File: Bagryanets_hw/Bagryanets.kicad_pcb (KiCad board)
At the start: 2 copper layers, 60 x 79 mm, 108 parts, among them U1 SX1276

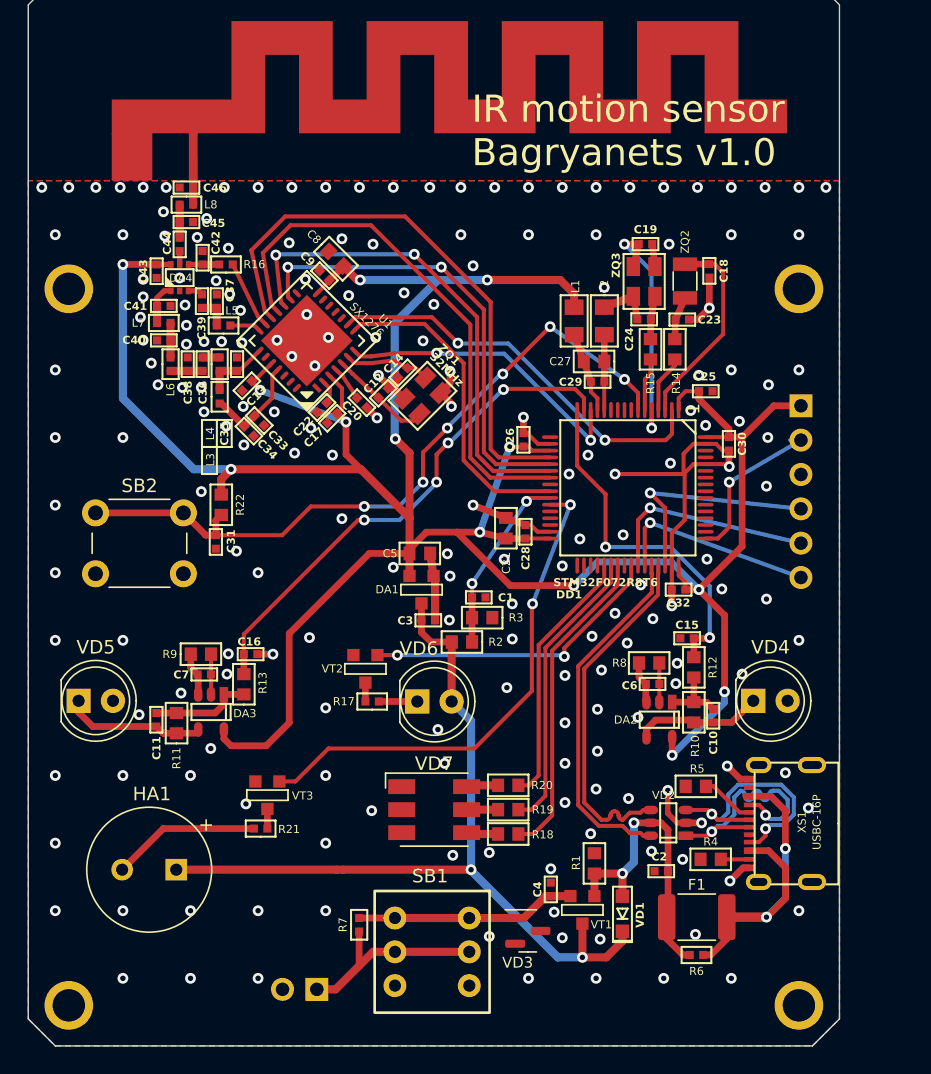
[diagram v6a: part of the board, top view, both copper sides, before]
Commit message: Added bom, small schematic changes
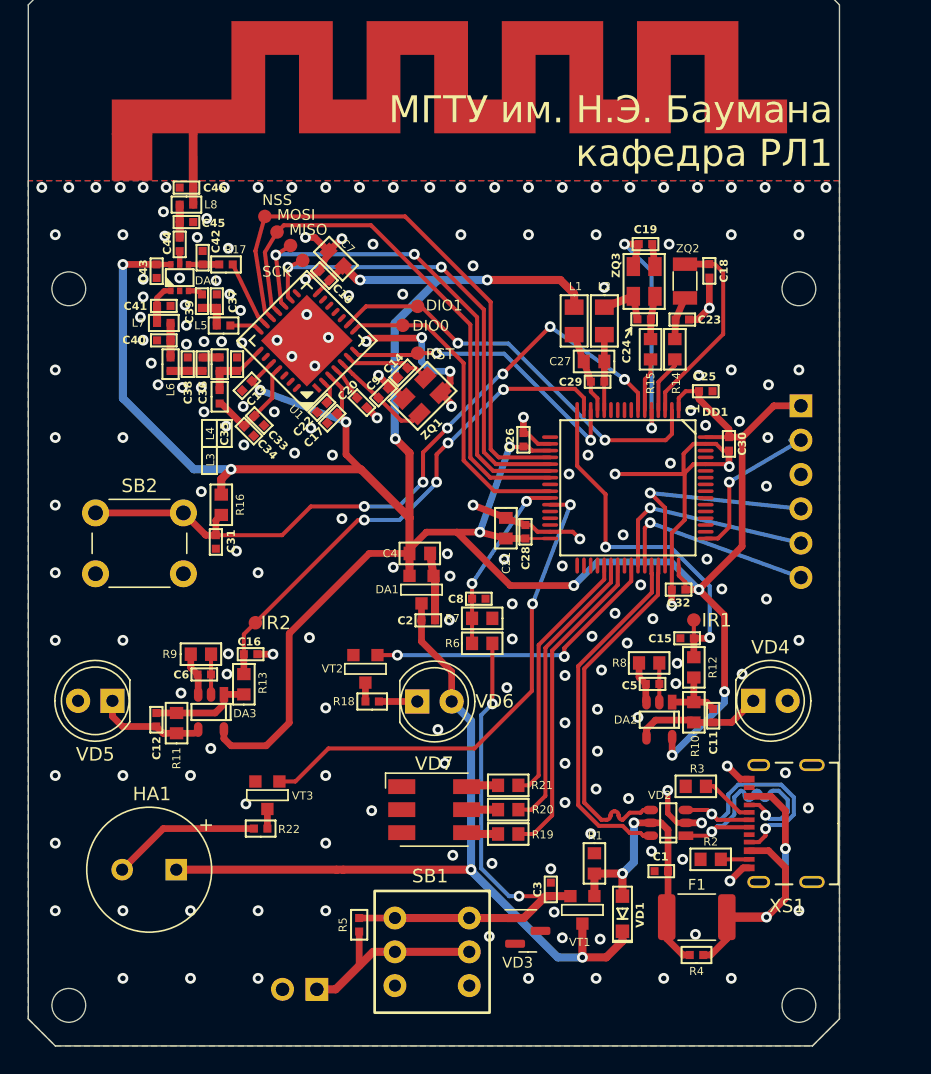
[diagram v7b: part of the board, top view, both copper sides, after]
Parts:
- removed the C1 at (141.3, 96.8)
- removed the R2 at (140.1, 100.1)
- removed the R3 at (141.6, 98.3)
- added C8: 100n, Capacitors:CAP_0402, F.Cu at (141.3, 96.9)
- added R6: 100k, Resistors:RES_0603, F.Cu at (141.6, 100.2)
- added R7: 100k, Resistors:RES_0603, F.Cu at (141.6, 98.4)
- added TP1: TestPoint, PCB:TESTPOINT_1MM, F.Cu at (157.2, 98.5)
- added TP2: TestPoint, PCB:TESTPOINT_1MM, F.Cu at (124.8, 98.7)
- added TP3: TestPoint, PCB:TESTPOINT_1MM, F.Cu at (135.7, 76.7)
- added TP4: TestPoint, PCB:TESTPOINT_1MM, F.Cu at (136.8, 75.3)
- added TP5: TestPoint, PCB:TESTPOINT_1MM, F.Cu at (128.3, 71.9)
- added TP6: TestPoint, PCB:TESTPOINT_1MM, F.Cu at (127.4, 70.8)
- added TP7: TestPoint, PCB:TESTPOINT_1MM, F.Cu at (126.4, 69.8)
- added TP8: TestPoint, PCB:TESTPOINT_1MM, F.Cu at (125.5, 68.7)
- added TP9: TestPoint, PCB:TESTPOINT_1MM, F.Cu at (136.8, 78.8)
- C14, C19, C24: value 10p -> 8p
- C18, C23: value 12.5p -> 9p
- C9: renamed from C12; value 10p -> 8p
- H1, H2, H3, H4: footprint Kais_Lib:Hole_2.4 -> MountingHole:MountingHole_2.5mm
- R22: renamed from R21; value 200 -> 510
- moved VD5 2.50 mm to (114.2, 104.5), turned to 180 degrees
- renumbered C2 to C1, C9 to C10, C10 to C11, C11 to C12, C3 to C2, C4 to C3, C5 to C4, C6 to C5, C7 to C6, C8 to C7, R22 to R16, R16 to R17, R17 to R18, R18 to R19, R4 to R2, R19 to R20, R20 to R21, R5 to R3, R6 to R4, R7 to R5
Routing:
- net /Battery: track 16.3 -> 39.3 mm, vias 0 -> 2
- net GND: track 73.9 -> 91.0 mm, vias 194 -> 192
- net Net-(DA3--): track 10.5 -> 8.13 mm
- net /IR_IN2: track 26.3 -> 27.6 mm
- net /L.MISO: track 36.8 -> 38.1 mm
- net /L.SCK: track 34.1 -> 35.3 mm
- net /Unst.power: track 61.6 -> 60.7 mm
- net /L.DIO1: track 29.9 -> 30.6 mm
- net /L.NSS: track 42.2 -> 42.8 mm
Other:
- board text added: "3.3 B"
- board text added: "DIO0"
- board text added: "DIO1"
- board text added: "GND"
- board text added: "IR1"
- board text added: "IR2"
- board text added: "MISO"
- board text added: "MOSI"
- board text added: "NSS"
- board text added: "RST"
- board text added: "SCK"
- board text added: "SWCLK"
- board text added: "SWDIO"
- board text added: "UART RX"
- board text added: "UART TX"
- board text added: "МГТУ им. Н.Э. Баумана кафедра РЛ1"

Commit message: Schematic update, IR amplifier working
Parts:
- C11, C12: value 1p* -> 8p
- DA1: value MCP1700-3302E_SOT23 -> MCP1700-3302
- DA2, DA3: value LMV721M5 -> MCP6001UT-I/OT
- VD2: value USBLC6_2SC6 -> USBLC6-2SC6
- VD4, VD5: value BL-L515 -> SFH213FA
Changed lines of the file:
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@@
         (effects (font (size 0.6 0.6) (thickness 0.15) bold))
     )
-    (fp_text value "1p*" (at 0 1.15 90) (layer "F.SilkS") hide
+    (fp_text value "8p" (at 0 1.15 90) (layer "F.SilkS") hide
         (effects (font (size 0.6 0.6) (thickness 0.15)))
     )
@@
         (effects (font (size 0.6 0.6) (thickness 0.15)))
     )
-    (fp_text value "MCP1700-3302E_SOT23" (at 0.25 -2.39942) (layer "F.SilkS") hide
+    (fp_text value "MCP1700-3302" (at 0.25 -2.39942) (layer "F.SilkS") hide
         (effects (font (size 0.6 0.6) (thickness 0.15) bold))
     )
@@
         (effects (font (size 1 1) (thickness 0.15)))
     )
-    (fp_text value "BL-L515" (at 1.27 3.96) (layer "F.Fab")
+    (fp_text value "SFH213FA" (at 1.27 3.96) (layer "F.Fab")
         (effects (font (size 1 1) (thickness 0.15)))
     )
@@
         (effects (font (size 0.6 0.6) (thickness 0.15) bold))
     )
-    (fp_text value "1p*" (at 0 1.15 90) (layer "F.SilkS") hide
+    (fp_text value "8p" (at 0 1.15 90) (layer "F.SilkS") hide
         (effects (font (size 0.6 0.6) (thickness 0.15)))
     )
@@
         (effects (font (size 0.6 0.6) (thickness 0.15)))
     )
-    (fp_text value "USBLC6_2SC6" (at -0.127 2.413 90) (layer "F.SilkS") hide
+    (fp_text value "USBLC6-2SC6" (at -0.127 2.413 90) (layer "F.SilkS") hide
         (effects (font (size 0.6 0.6) (thickness 0.15)))
     )
@@
         (effects (font (size 0.6 0.6) (thickness 0.15)))
     )
-    (fp_text value "LMV721M5" (at -0.127 2.413) (layer "F.SilkS") hide
+    (fp_text value "MCP6001UT-I/OT" (at -0.127 2.413) (layer "F.SilkS") hide
         (effects (font (size 0.6 0.6) (thickness 0.15) bold))
     )
@@
         (effects (font (size 0.6 0.6) (thickness 0.15)))
     )
-    (fp_text value "LMV721M5" (at -2.327 2.013) (layer "F.SilkS") hide
+    (fp_text value "MCP6001UT-I/OT" (at -2.327 2.013) (layer "F.SilkS") hide
         (effects (font (size 0.6 0.6) (thickness 0.15) bold))
     )
@@
         (effects (font (size 1 1) (thickness 0.15)))
     )
-    (fp_text value "BL-L515" (at 1.27 3.96) (layer "F.Fab")
+    (fp_text value "SFH213FA" (at 1.27 3.96) (layer "F.Fab")
         (effects (font (size 1 1) (thickness 0.15)))
     )
